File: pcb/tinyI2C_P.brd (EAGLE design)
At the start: 83.2 x 83.2 mm, 274 parts, among them IC1 74LVC1G125DCK, IC10 74LVC1G125DCK, IC11 74LVC1G125DCK, IC12 IC_LDO_MIC5355, IC13 74LVC1G125DCK, IC14 74LVC1G125DCK, IC15 IC_LDO_MIC5355, IC16 74LVC1G125DCK, IC17 74LVC1G125DCK, IC18 IC_LDO_MIC5355, IC19 74LVC1G125DCK, IC2 74LVC1G125DCK, IC20 74LVC1G125DCK, IC21 IC_LDO_MIC5355, IC22 74LVC1G125DCK, IC23 74LVC1G125DCK, IC24 IC_LDO_MIC5355, IC3 IC_LDO_MIC5355, IC4 74LVC1G125DCK, IC5 74LVC1G125DCK, IC6 IC_LDO_MIC5355, IC7 74LVC1G125DCK, IC8 74LVC1G125DCK, IC9 IC_LDO_MIC5355, U1 LPC824M201JHI33, U2 LPC824M201JHI33, U3 LPC824M201JHI33, U4 LPC824M201JHI33, U5 LPC824M201JHI33, U6 LPC824M201JHI33, U7 LPC824M201JHI33, U8 LPC824M201JHI33, X1 TSW-112-02-S-S, X10 TSW-102-02-S-S, X11 TSW-102-02-S-S, X12 TSW-102-02-S-S, X13 TSW-106-02-S-S-RA, X14 TSW-112-02-S-S, X15 TSW-112-02-S-S, X16 TSW-102-02-S-S, X17 TSW-102-02-S-S, X18 TSW-102-02-S-S, X19 TSW-106-02-S-S-RA, X2 TSW-112-02-S-S, X20 TSW-112-02-S-S, X21 TSW-112-02-S-S, X22 TSW-102-02-S-S, X23 TSW-102-02-S-S, X24 TSW-102-02-S-S, X25 TSW-106-02-S-S-RA, X26 TSW-112-02-S-S, X27 TSW-112-02-S-S, X28 TSW-102-02-S-S, X29 TSW-102-02-S-S, X3 TSW-106-02-S-S-RA, X30 TSW-102-02-S-S, X31 TSW-106-02-S-S-RA, X32 TSW-112-02-S-S, X33 TSW-112-02-S-S, X34 TSW-102-02-S-S, X35 TSW-102-02-S-S, X36 TSW-102-02-S-S, X37 TSW-106-02-S-S-RA, X38 TSW-112-02-S-S, X39 TSW-112-02-S-S, X4 TSW-102-02-S-S, X40 TSW-102-02-S-S, X41 TSW-102-02-S-S, X42 TSW-102-02-S-S, X43 TSW-106-02-S-S-RA, X44 TSW-112-02-S-S, X45 TSW-112-02-S-S, X46 TSW-102-02-S-S, X47 TSW-102-02-S-S, X48 TSW-102-02-S-S, X5 TSW-102-02-S-S, X6 TSW-102-02-S-S, X7 TSW-106-02-S-S-RA, X8 TSW-112-02-S-S, X9 TSW-112-02-S-S

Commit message: [ PCB ] panelised
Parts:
- added I1, I2, I3, I4, I5, I6, I7, I8: ICON_MINLAB_5.2S, mylib:ICON_MINLAB_5.2MM
- added TP35, TP37, TP39, TP40, TP42: TPTP07R, testpad_local:TP07R
- added TP36, TP38, TP41, TP43: TPB1,27, testpad_local:B1,27
- C1, C10, C11, C15, C16, C19, C2, C20, C24, C25, C28, C29, C33, C34, C37, C38, C42, C43, C46, C47, C51, C52, C55, C56, C6, C60, C61, C64, C65, C69, C7, C70: value 1005 -> 0.1u/1005
- C12, C13, C14, C21, C22, C23, C3, C30, C31, C32, C39, C4, C40, C41, C48, C49, C5, C50, C57, C58, C59, C66, C67, C68: value 1005 -> 10u/1005
- C17, C18, C26, C27, C35, C36, C44, C45, C53, C54, C62, C63, C71, C72, C8, C9: value 1005 -> 18p/1005
- IC12, IC15, IC18, IC21, IC24, IC3, IC6, IC9: device mylib:IC_08_0.65_160MIL -> mylib:IC_08_0.65_160MIL_EP
- Q1, Q2, Q3, Q4, Q5, Q6, Q7, Q8: value (none) -> 12MHz
- TP11, TP13, TP16, TP18, TP21, TP23, TP26, TP28, TP3, TP31, TP33, TP7: value TPTP07R -> TPB1,27; device testpad_local:TP07R -> testpad_local:B1,27
- TP4, TP5: value TPTP10R -> TPTP20R; device testpad:TP10R -> testpad_local:TP20R
- TP8: value TPTP07R -> TPTP20R; device testpad_local:TP07R -> testpad_local:TP20R
- moved TP34 77.2 mm to (81.7, 36.2)
- moved C72 75.3 mm to (83.0, 46.1)
- moved U8 75.2 mm to (85.5, 55.5)
- moved C71 75.1 mm to (82.5, 51.5)
- moved IC23 75.0 mm to (89.8, 64.9), turned to 270 degrees
- moved R74 74.8 mm to (87.6, 61.2)
- moved R73 74.8 mm to (87.6, 59.8)
- moved IC24 74.7 mm to (80.2, 64.7)
- moved C65 74.5 mm to (84.7, 50.3)
- moved C67 74.5 mm to (78.2, 66.9)
- moved R79 74.5 mm to (78.0, 46.8)
- moved C66 74.5 mm to (83.2, 62.6)
- moved C70 74.5 mm to (85.6, 66.8)
- moved IC22 74.5 mm to (87.1, 65.2)
- moved R71 74.5 mm to (78.0, 61.2)
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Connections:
- net 1.8V1: now also TP10.TP; no longer TP8.TP
- net 1.8V2: now also TP15.TP; no longer TP12.TP
- net 1.8V3: now also TP20.TP; no longer TP16.TP
- net 1.8V4: now also TP25.TP; no longer TP20.TP
- net 1.8V5: now also TP30.TP; no longer TP24.TP
- net 1.8V6: now also TP35.TP; no longer TP28.TP
- net 1.8V7: now also TP40.TP; no longer TP32.TP
- net 3.3V1: now also TP12.TP; no longer TP10.TP
- net 3.3V2: now also TP17.TP; no longer TP14.TP
- net 3.3V3: now also TP22.TP; no longer TP18.TP
- net 3.3V4: now also TP27.TP; no longer TP22.TP
- net 3.3V5: now also TP32.TP; no longer TP26.TP
- net 3.3V6: now also TP37.TP; no longer TP30.TP
- net 3.3V7: now also TP42.TP; no longer TP34.TP
- net 5V1: now also TP9.TP; no longer TP7.TP
- net 5V2: now also TP14.TP; no longer TP11.TP
- net 5V3: now also TP19.TP; no longer TP15.TP
- net 5V4: now also TP24.TP; no longer TP19.TP
- net 5V5: now also TP29.TP; no longer TP23.TP
- net 5V6: now also TP34.TP; no longer TP27.TP
- net 5V7: now also TP39.TP; no longer TP31.TP
- net GND: now also IC3.3, IC3.6, TP7.TP
- net GND1: now also IC6.3, IC6.6, TP11.TP, TP13.TP; no longer TP9.TP
- net GND2: now also IC9.3, IC9.6, TP16.TP, TP18.TP; no longer TP13.TP
- net GND3: now also IC12.3, IC12.6, TP21.TP, TP23.TP; no longer TP17.TP
- net GND4: now also IC15.3, IC15.6, TP26.TP, TP28.TP; no longer TP21.TP
- net GND5: now also IC18.3, IC18.6, TP31.TP, TP33.TP; no longer TP25.TP
- net GND6: now also IC21.3, IC21.6, TP36.TP, TP38.TP; no longer TP29.TP
- net GND7: now also IC24.3, IC24.6, TP41.TP, TP43.TP; no longer TP33.TP
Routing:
- net 1.8V3: track 39.1 -> 88.4 mm
- net 1.8V: track 39.1 -> 88.4 mm
- net 1.8V2: track 39.1 -> 88.4 mm
- net 1.8V1: track 39.1 -> 88.4 mm
- net 1.8V7: track 39.1 -> 88.4 mm
- net 1.8V4: track 39.1 -> 88.4 mm
- net 1.8V6: track 39.1 -> 88.4 mm
- net 1.8V5: track 39.1 -> 88.4 mm
- net TX->6: track 5.96 -> 12.5 mm
- net TX->7: track 5.96 -> 12.5 mm
- net TX->4: track 5.96 -> 12.5 mm
- net TX->3: track 5.96 -> 12.5 mm
- net TX->5: track 5.96 -> 12.5 mm
- net TX->2: track 5.96 -> 12.5 mm
- net TX->1: track 5.96 -> 12.5 mm
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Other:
- board size 83.2 x 83.2 mm -> 100 x 84.4 mm
- board text added: "GND"
- board text added: "Q1"
- board text added: "V-CUT"

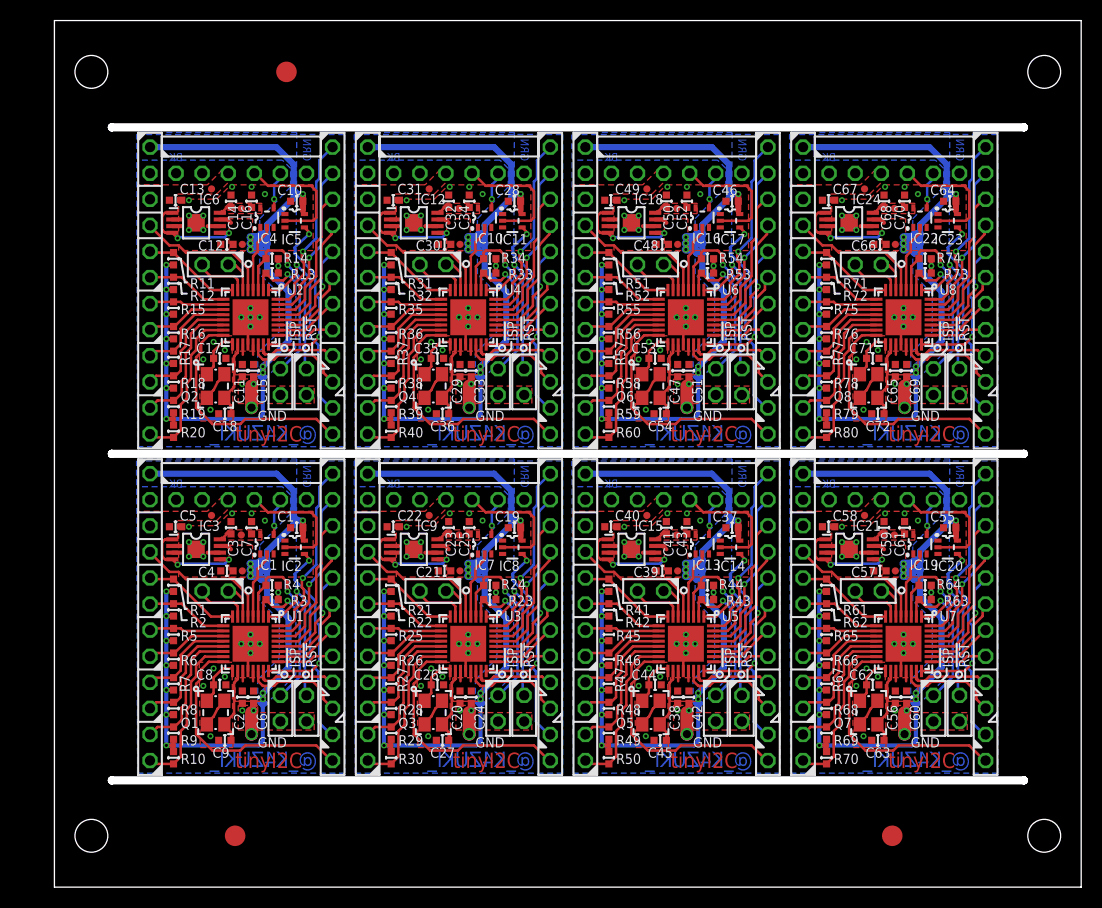
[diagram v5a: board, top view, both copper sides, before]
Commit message: [ PCB ] panel/drill size change, V-CUT mark, Panelize
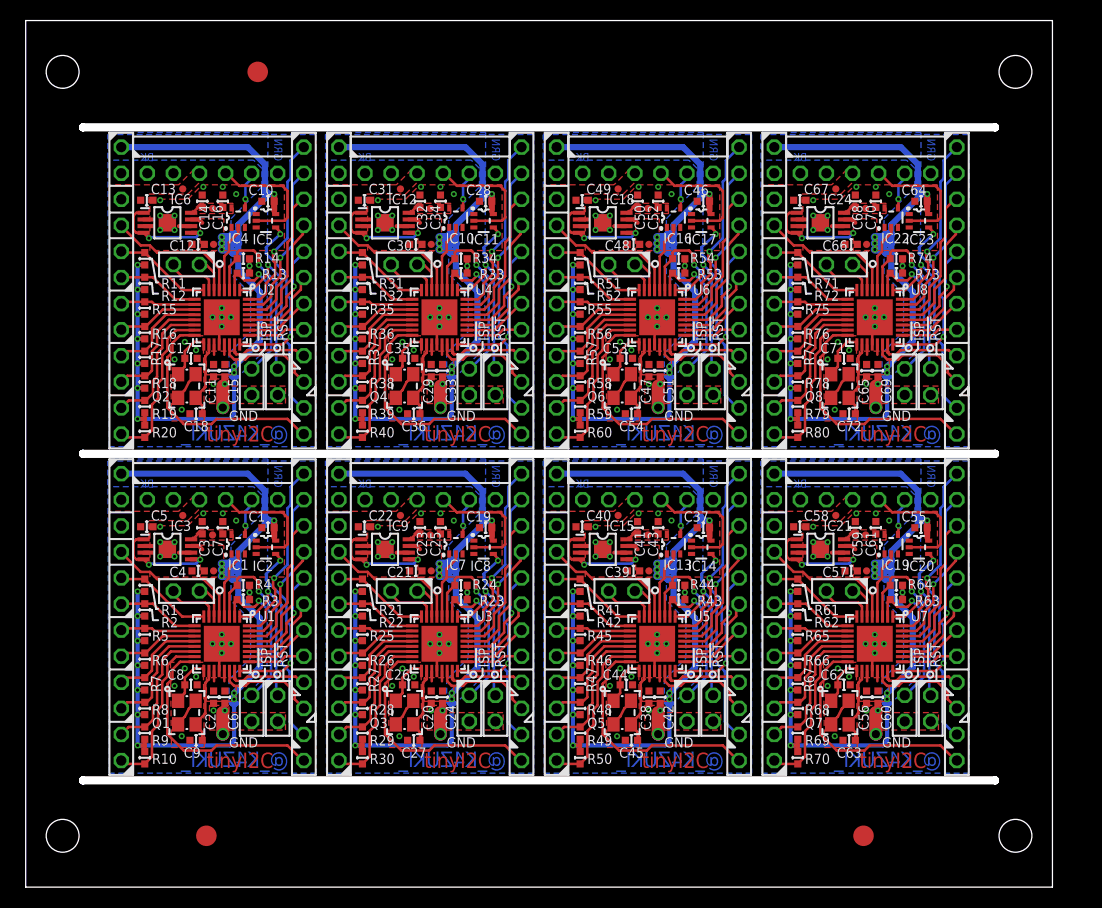
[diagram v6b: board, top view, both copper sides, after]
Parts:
- moved TP5 2.80 mm to (81.6, 5.00)
- moved X27 2.80 mm to (69.5, 26.3)
- moved X33 2.80 mm to (69.5, 58.1)
- moved C19 2.80 mm to (44.8, 35.0)
- moved C23 2.80 mm to (38.4, 35.0)
- moved C25 2.80 mm to (40.4, 35.0)
- moved C26 2.80 mm to (37.3, 19.7)
- moved C27 2.80 mm to (37.8, 14.3)
- moved C28 2.80 mm to (44.8, 66.8)
- moved C32 2.80 mm to (38.4, 66.8)
- moved C34 2.80 mm to (40.4, 66.8)
- moved C35 2.80 mm to (37.3, 51.5)
- moved C36 2.80 mm to (37.8, 46.1)
- moved C43 2.80 mm to (61.6, 35.0)
- moved C52 2.80 mm to (61.6, 66.8)
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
